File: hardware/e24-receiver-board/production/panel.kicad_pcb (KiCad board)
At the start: 2 copper layers, 40 x 56.4 mm, 199 parts, among them J1 505070-2422, J10 SPEAKER-, J11 GND1, J12 TRACK_RIGHT, J13 MOTOR+, J14 LAMP_REAR, J15 CAP+, J16 U+, J17 AUX3, J18 AUX10, J19 AUX12, J2 TRACK_LEFT, J20 SPEAKER+, J21 GND2, J3 MOTOR-, J4 LAMP_FRONT, J5 VCC, J6 AUX1, J7 AUX2, J8 AUX4, J9 AUX11

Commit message: chore: add hardware revision and date codes
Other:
- board text added: "v0.1.0"

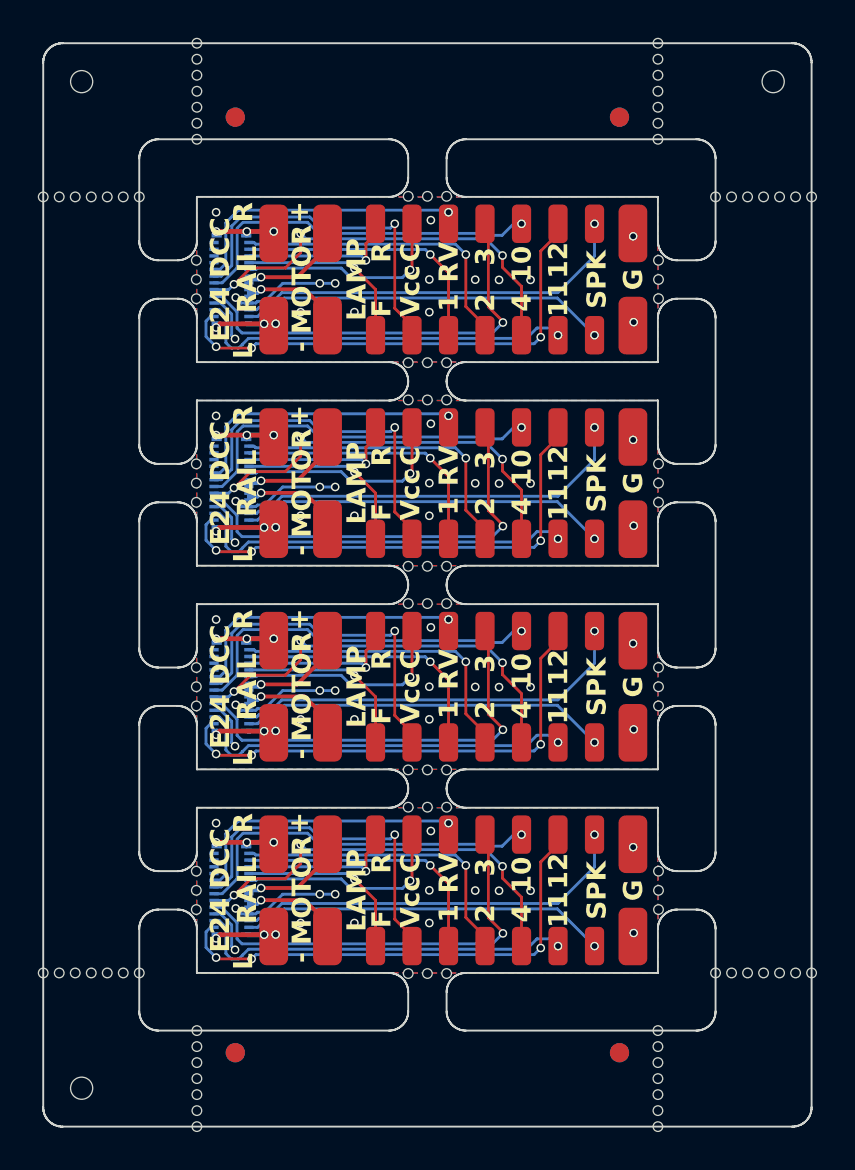
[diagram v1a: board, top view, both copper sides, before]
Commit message: fix: update to kicad 9.0
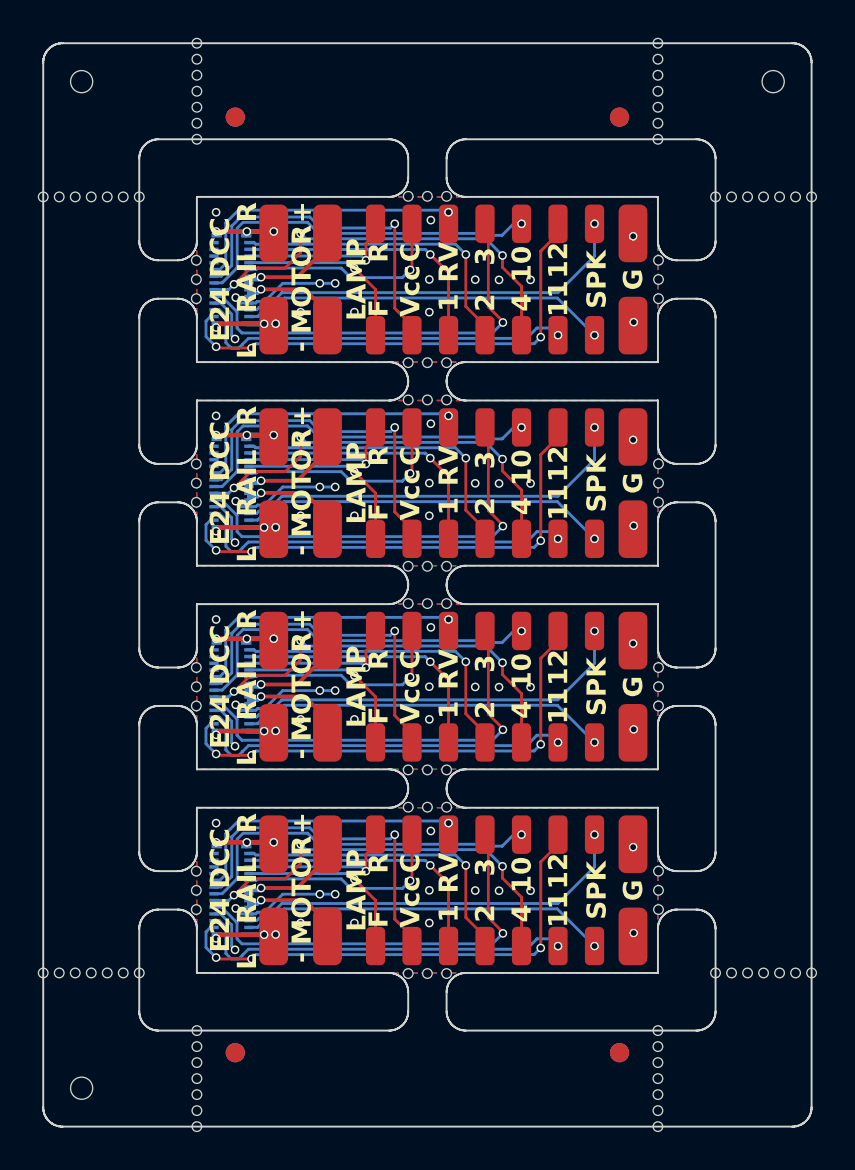
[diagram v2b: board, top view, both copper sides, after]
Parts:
- removed the J1 at (138.3, 64.1)
- removed the J1 at (138.3, 32.3)
- removed the J1 at (138.3, 53.5)
- removed the J1 at (138.3, 42.9)
- removed the J10 at (157.2, 67.0)
- removed the J10 at (157.2, 56.4)
- removed the J10 at (157.2, 35.2)
- removed the J10 at (157.2, 45.8)
- removed the J11 at (159.2, 45.3)
- removed the J11 at (159.2, 66.5)
- removed the J11 at (159.2, 55.9)
- removed the J11 at (159.2, 34.7)
- removed the J12 at (140.5, 61.7)
- removed the J12 at (140.5, 40.5)
- removed the J12 at (140.5, 51.1)
- removed the J12 at (140.5, 29.9)
- removed the J13 at (143.3, 61.7)
- removed the J13 at (143.3, 51.1)
- removed the J13 at (143.3, 29.9)
- removed the J13 at (143.3, 40.5)
- removed the J14 at (145.8, 50.6)
- removed the J14 at (145.8, 29.4)
- removed the J14 at (145.8, 61.2)
- removed the J14 at (145.8, 40.0)
- removed the J15 at (147.7, 61.2)
- removed the J15 at (147.7, 29.4)
- removed the J15 at (147.7, 40.0)
- removed the J15 at (147.7, 50.6)
- removed the J16 at (149.6, 50.6)
- removed the J16 at (149.6, 40.0)
- removed the J16 at (149.6, 29.4)
- removed the J16 at (149.6, 61.2)
- removed the J17 at (151.5, 61.2)
- removed the J17 at (151.5, 50.6)
- removed the J17 at (151.5, 40.0)
- removed the J17 at (151.5, 29.4)
- removed the J18 at (153.4, 50.6)
- removed the J18 at (153.4, 29.4)
- removed the J18 at (153.4, 40.0)
- removed the J18 at (153.4, 61.2)
- removed the J19 at (155.3, 29.4)
- removed the J19 at (155.3, 50.6)
- removed the J19 at (155.3, 40.0)
- removed the J19 at (155.3, 61.2)
- removed the J2 at (140.5, 66.5)
- removed the J2 at (140.5, 45.3)
- removed the J2 at (140.5, 55.9)
- removed the J2 at (140.5, 34.7)
- removed the J20 at (157.2, 40.0)
- removed the J20 at (157.2, 29.4)
- removed the J20 at (157.2, 61.2)
- removed the J20 at (157.2, 50.6)
- removed the J21 at (159.2, 40.5)
- removed the J21 at (159.2, 51.1)
- removed the J21 at (159.2, 29.9)
- removed the J21 at (159.2, 61.7)
- removed the J3 at (143.3, 45.3)
- removed the J3 at (143.3, 34.7)
- removed the J3 at (143.3, 55.9)
- removed the J3 at (143.3, 66.5)
- removed the J4 at (145.8, 67.0)
- removed the J4 at (145.8, 35.2)
- removed the J4 at (145.8, 56.4)
- removed the J4 at (145.8, 45.8)
- removed the J5 at (147.7, 56.4)
- removed the J5 at (147.7, 45.8)
- removed the J5 at (147.7, 67.0)
- removed the J5 at (147.7, 35.2)
- removed the J6 at (149.6, 67.0)
- removed the J6 at (149.6, 45.8)
- removed the J6 at (149.6, 35.2)
- removed the J6 at (149.6, 56.4)
- removed the J7 at (151.5, 35.2)
- removed the J7 at (151.5, 67.0)
- removed the J7 at (151.5, 45.8)
- removed the J7 at (151.5, 56.4)
- removed the J8 at (153.4, 45.8)
- removed the J8 at (153.4, 67.0)
- removed the J8 at (153.4, 56.4)
- removed the J8 at (153.4, 35.2)
- removed the J9 at (155.3, 45.8)
- removed the J9 at (155.3, 56.4)
- removed the J9 at (155.3, 35.2)
- removed the J9 at (155.3, 67.0)
- added J1: 505070-2422, e24-receiver-board:CONN-SMD_24P-P0.35_5050702422, B.Cu at (138.3, 53.5)
- added J1: 505070-2422, e24-receiver-board:CONN-SMD_24P-P0.35_5050702422, B.Cu at (138.3, 42.9)
- added J1: 505070-2422, e24-receiver-board:CONN-SMD_24P-P0.35_5050702422, B.Cu at (138.3, 32.3)
- added J1: 505070-2422, e24-receiver-board:CONN-SMD_24P-P0.35_5050702422, B.Cu at (138.3, 64.1)
- added J10: SPEAKER-, e24-receiver-board:SolderWirePad_1x01_SMD_1x2mm, F.Cu at (157.2, 56.4)
- added J10: SPEAKER-, e24-receiver-board:SolderWirePad_1x01_SMD_1x2mm, F.Cu at (157.2, 67.0)
- added J10: SPEAKER-, e24-receiver-board:SolderWirePad_1x01_SMD_1x2mm, F.Cu at (157.2, 45.8)
- added J10: SPEAKER-, e24-receiver-board:SolderWirePad_1x01_SMD_1x2mm, F.Cu at (157.2, 35.2)
- added J11: GND1, e24-receiver-board:SolderWirePad_1x01_SMD_1.5x3mm, F.Cu at (159.2, 45.3)
- added J11: GND1, e24-receiver-board:SolderWirePad_1x01_SMD_1.5x3mm, F.Cu at (159.2, 55.9)
- added J11: GND1, e24-receiver-board:SolderWirePad_1x01_SMD_1.5x3mm, F.Cu at (159.2, 66.5)
- added J11: GND1, e24-receiver-board:SolderWirePad_1x01_SMD_1.5x3mm, F.Cu at (159.2, 34.7)
- added J12: TRACK_RIGHT, e24-receiver-board:SolderWirePad_1x01_SMD_1.5x3mm, F.Cu at (140.5, 29.9)
- added J12: TRACK_RIGHT, e24-receiver-board:SolderWirePad_1x01_SMD_1.5x3mm, F.Cu at (140.5, 51.1)
- added J12: TRACK_RIGHT, e24-receiver-board:SolderWirePad_1x01_SMD_1.5x3mm, F.Cu at (140.5, 40.5)
- added J12: TRACK_RIGHT, e24-receiver-board:SolderWirePad_1x01_SMD_1.5x3mm, F.Cu at (140.5, 61.7)
- added J13: MOTOR+, e24-receiver-board:SolderWirePad_1x01_SMD_1.5x3mm, F.Cu at (143.3, 51.1)
- added J13: MOTOR+, e24-receiver-board:SolderWirePad_1x01_SMD_1.5x3mm, F.Cu at (143.3, 40.5)
- added J13: MOTOR+, e24-receiver-board:SolderWirePad_1x01_SMD_1.5x3mm, F.Cu at (143.3, 29.9)
- added J13: MOTOR+, e24-receiver-board:SolderWirePad_1x01_SMD_1.5x3mm, F.Cu at (143.3, 61.7)
- added J14: LAMP_REAR, e24-receiver-board:SolderWirePad_1x01_SMD_1x2mm, F.Cu at (145.8, 40.0)
- added J14: LAMP_REAR, e24-receiver-board:SolderWirePad_1x01_SMD_1x2mm, F.Cu at (145.8, 61.2)
- added J14: LAMP_REAR, e24-receiver-board:SolderWirePad_1x01_SMD_1x2mm, F.Cu at (145.8, 50.6)
- added J14: LAMP_REAR, e24-receiver-board:SolderWirePad_1x01_SMD_1x2mm, F.Cu at (145.8, 29.4)
- added J15: CAP+, e24-receiver-board:SolderWirePad_1x01_SMD_1x2mm, F.Cu at (147.7, 61.2)
- added J15: CAP+, e24-receiver-board:SolderWirePad_1x01_SMD_1x2mm, F.Cu at (147.7, 50.6)
- added J15: CAP+, e24-receiver-board:SolderWirePad_1x01_SMD_1x2mm, F.Cu at (147.7, 40.0)
- added J15: CAP+, e24-receiver-board:SolderWirePad_1x01_SMD_1x2mm, F.Cu at (147.7, 29.4)
- added J16: U+, e24-receiver-board:SolderWirePad_1x01_SMD_1x2mm, F.Cu at (149.6, 29.4)
- added J16: U+, e24-receiver-board:SolderWirePad_1x01_SMD_1x2mm, F.Cu at (149.6, 40.0)
- added J16: U+, e24-receiver-board:SolderWirePad_1x01_SMD_1x2mm, F.Cu at (149.6, 61.2)
- added J16: U+, e24-receiver-board:SolderWirePad_1x01_SMD_1x2mm, F.Cu at (149.6, 50.6)
- added J17: AUX3, e24-receiver-board:SolderWirePad_1x01_SMD_1x2mm, F.Cu at (151.5, 40.0)
- added J17: AUX3, e24-receiver-board:SolderWirePad_1x01_SMD_1x2mm, F.Cu at (151.5, 29.4)
- added J17: AUX3, e24-receiver-board:SolderWirePad_1x01_SMD_1x2mm, F.Cu at (151.5, 50.6)
- added J17: AUX3, e24-receiver-board:SolderWirePad_1x01_SMD_1x2mm, F.Cu at (151.5, 61.2)
- added J18: AUX10, e24-receiver-board:SolderWirePad_1x01_SMD_1x2mm, F.Cu at (153.4, 50.6)
- added J18: AUX10, e24-receiver-board:SolderWirePad_1x01_SMD_1x2mm, F.Cu at (153.4, 40.0)
- added J18: AUX10, e24-receiver-board:SolderWirePad_1x01_SMD_1x2mm, F.Cu at (153.4, 61.2)
- added J18: AUX10, e24-receiver-board:SolderWirePad_1x01_SMD_1x2mm, F.Cu at (153.4, 29.4)
- added J19: AUX12, e24-receiver-board:SolderWirePad_1x01_SMD_1x2mm, F.Cu at (155.3, 61.2)
- added J19: AUX12, e24-receiver-board:SolderWirePad_1x01_SMD_1x2mm, F.Cu at (155.3, 50.6)
- added J19: AUX12, e24-receiver-board:SolderWirePad_1x01_SMD_1x2mm, F.Cu at (155.3, 29.4)
- added J19: AUX12, e24-receiver-board:SolderWirePad_1x01_SMD_1x2mm, F.Cu at (155.3, 40.0)
- added J2: TRACK_LEFT, e24-receiver-board:SolderWirePad_1x01_SMD_1.5x3mm, F.Cu at (140.5, 34.7)
- added J2: TRACK_LEFT, e24-receiver-board:SolderWirePad_1x01_SMD_1.5x3mm, F.Cu at (140.5, 55.9)
- added J2: TRACK_LEFT, e24-receiver-board:SolderWirePad_1x01_SMD_1.5x3mm, F.Cu at (140.5, 45.3)
- added J2: TRACK_LEFT, e24-receiver-board:SolderWirePad_1x01_SMD_1.5x3mm, F.Cu at (140.5, 66.5)
- added J20: SPEAKER+, e24-receiver-board:SolderWirePad_1x01_SMD_1x2mm, F.Cu at (157.2, 40.0)
- added J20: SPEAKER+, e24-receiver-board:SolderWirePad_1x01_SMD_1x2mm, F.Cu at (157.2, 29.4)
- added J20: SPEAKER+, e24-receiver-board:SolderWirePad_1x01_SMD_1x2mm, F.Cu at (157.2, 50.6)
- added J20: SPEAKER+, e24-receiver-board:SolderWirePad_1x01_SMD_1x2mm, F.Cu at (157.2, 61.2)
- added J21: GND2, e24-receiver-board:SolderWirePad_1x01_SMD_1.5x3mm, F.Cu at (159.2, 51.1)
- added J21: GND2, e24-receiver-board:SolderWirePad_1x01_SMD_1.5x3mm, F.Cu at (159.2, 40.5)
- added J21: GND2, e24-receiver-board:SolderWirePad_1x01_SMD_1.5x3mm, F.Cu at (159.2, 29.9)
- added J21: GND2, e24-receiver-board:SolderWirePad_1x01_SMD_1.5x3mm, F.Cu at (159.2, 61.7)
- added J3: MOTOR-, e24-receiver-board:SolderWirePad_1x01_SMD_1.5x3mm, F.Cu at (143.3, 45.3)
- added J3: MOTOR-, e24-receiver-board:SolderWirePad_1x01_SMD_1.5x3mm, F.Cu at (143.3, 34.7)
- added J3: MOTOR-, e24-receiver-board:SolderWirePad_1x01_SMD_1.5x3mm, F.Cu at (143.3, 55.9)
- added J3: MOTOR-, e24-receiver-board:SolderWirePad_1x01_SMD_1.5x3mm, F.Cu at (143.3, 66.5)
- added J4: LAMP_FRONT, e24-receiver-board:SolderWirePad_1x01_SMD_1x2mm, F.Cu at (145.8, 67.0)
- added J4: LAMP_FRONT, e24-receiver-board:SolderWirePad_1x01_SMD_1x2mm, F.Cu at (145.8, 56.4)
- added J4: LAMP_FRONT, e24-receiver-board:SolderWirePad_1x01_SMD_1x2mm, F.Cu at (145.8, 45.8)
- added J4: LAMP_FRONT, e24-receiver-board:SolderWirePad_1x01_SMD_1x2mm, F.Cu at (145.8, 35.2)
- added J5: VCC, e24-receiver-board:SolderWirePad_1x01_SMD_1x2mm, F.Cu at (147.7, 67.0)
- added J5: VCC, e24-receiver-board:SolderWirePad_1x01_SMD_1x2mm, F.Cu at (147.7, 56.4)
- added J5: VCC, e24-receiver-board:SolderWirePad_1x01_SMD_1x2mm, F.Cu at (147.7, 35.2)
- added J5: VCC, e24-receiver-board:SolderWirePad_1x01_SMD_1x2mm, F.Cu at (147.7, 45.8)
- added J6: AUX1, e24-receiver-board:SolderWirePad_1x01_SMD_1x2mm, F.Cu at (149.6, 45.8)
- added J6: AUX1, e24-receiver-board:SolderWirePad_1x01_SMD_1x2mm, F.Cu at (149.6, 67.0)
- added J6: AUX1, e24-receiver-board:SolderWirePad_1x01_SMD_1x2mm, F.Cu at (149.6, 35.2)
- added J6: AUX1, e24-receiver-board:SolderWirePad_1x01_SMD_1x2mm, F.Cu at (149.6, 56.4)
- added J7: AUX2, e24-receiver-board:SolderWirePad_1x01_SMD_1x2mm, F.Cu at (151.5, 45.8)
- added J7: AUX2, e24-receiver-board:SolderWirePad_1x01_SMD_1x2mm, F.Cu at (151.5, 67.0)
- added J7: AUX2, e24-receiver-board:SolderWirePad_1x01_SMD_1x2mm, F.Cu at (151.5, 56.4)
- added J7: AUX2, e24-receiver-board:SolderWirePad_1x01_SMD_1x2mm, F.Cu at (151.5, 35.2)
- added J8: AUX4, e24-receiver-board:SolderWirePad_1x01_SMD_1x2mm, F.Cu at (153.4, 45.8)
- added J8: AUX4, e24-receiver-board:SolderWirePad_1x01_SMD_1x2mm, F.Cu at (153.4, 35.2)
- added J8: AUX4, e24-receiver-board:SolderWirePad_1x01_SMD_1x2mm, F.Cu at (153.4, 67.0)
- added J8: AUX4, e24-receiver-board:SolderWirePad_1x01_SMD_1x2mm, F.Cu at (153.4, 56.4)
- added J9: AUX11, e24-receiver-board:SolderWirePad_1x01_SMD_1x2mm, F.Cu at (155.3, 67.0)
- added J9: AUX11, e24-receiver-board:SolderWirePad_1x01_SMD_1x2mm, F.Cu at (155.3, 35.2)
- added J9: AUX11, e24-receiver-board:SolderWirePad_1x01_SMD_1x2mm, F.Cu at (155.3, 56.4)
- added J9: AUX11, e24-receiver-board:SolderWirePad_1x01_SMD_1x2mm, F.Cu at (155.3, 45.8)
- turned KiKit_FID_B_1 to 180 degrees
- turned KiKit_FID_B_2 to 180 degrees
- turned KiKit_FID_B_3 to 180 degrees
- turned KiKit_FID_B_4 to 180 degrees
